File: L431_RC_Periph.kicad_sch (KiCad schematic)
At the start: 22 parts, among them J1 CAN1, J3 RC, T1 Tab, T2 Tab, T3 Tab, T4 Tab, U1 PCB

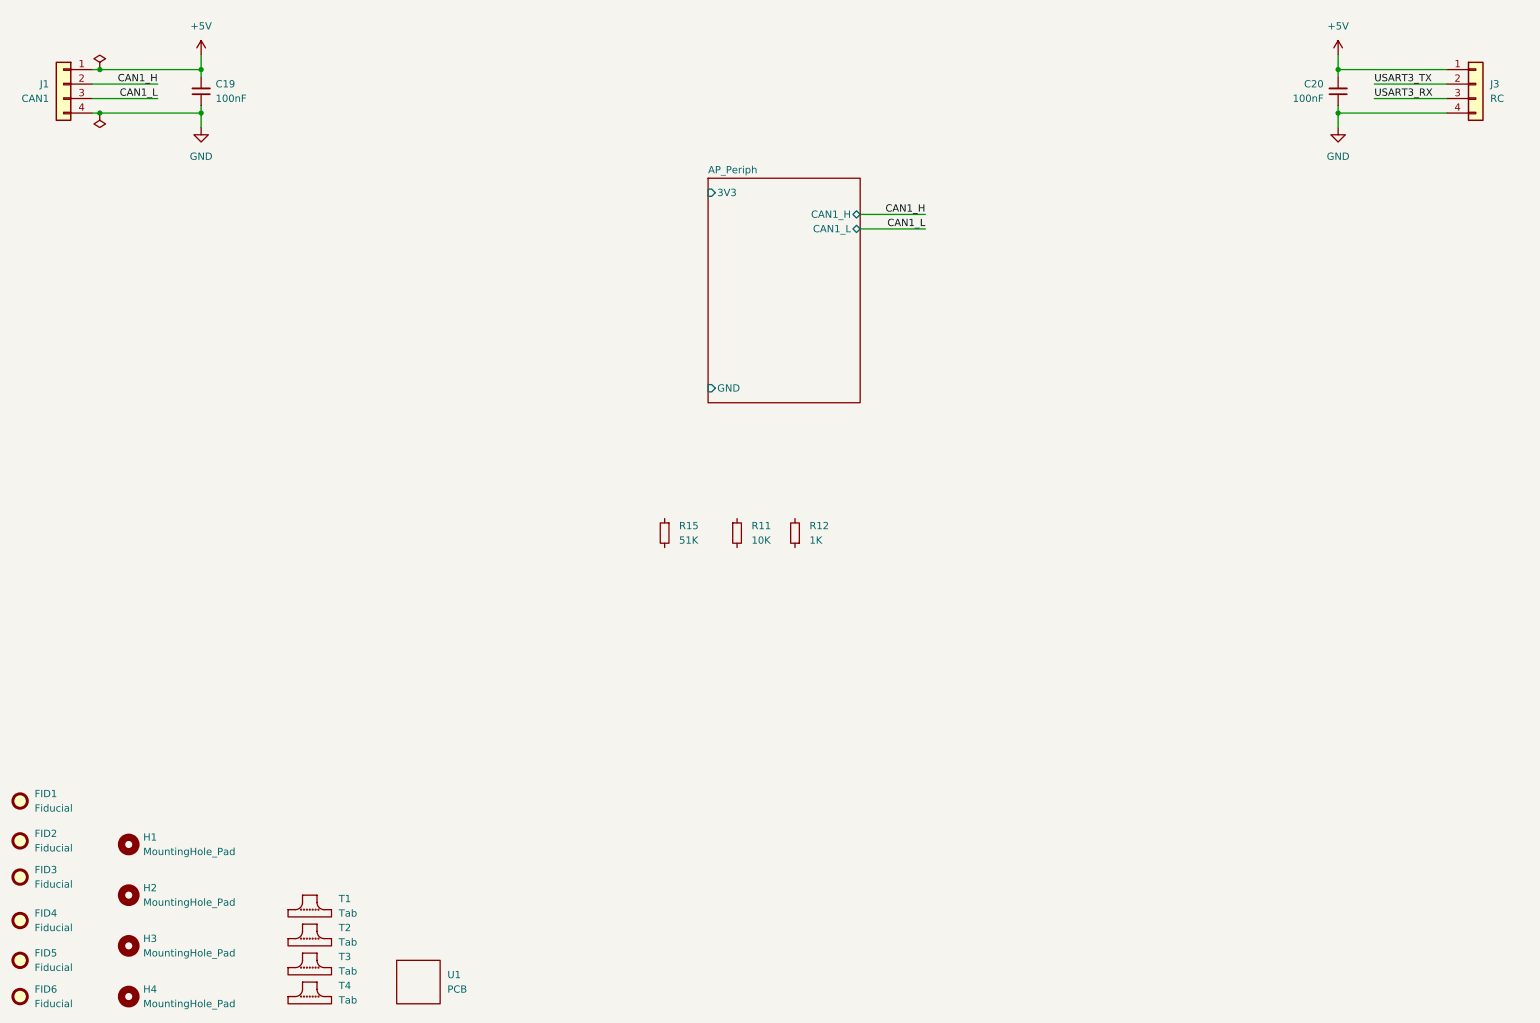
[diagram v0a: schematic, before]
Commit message: Finish routing and add option for using batt mon pads as I2C lines for added GPS
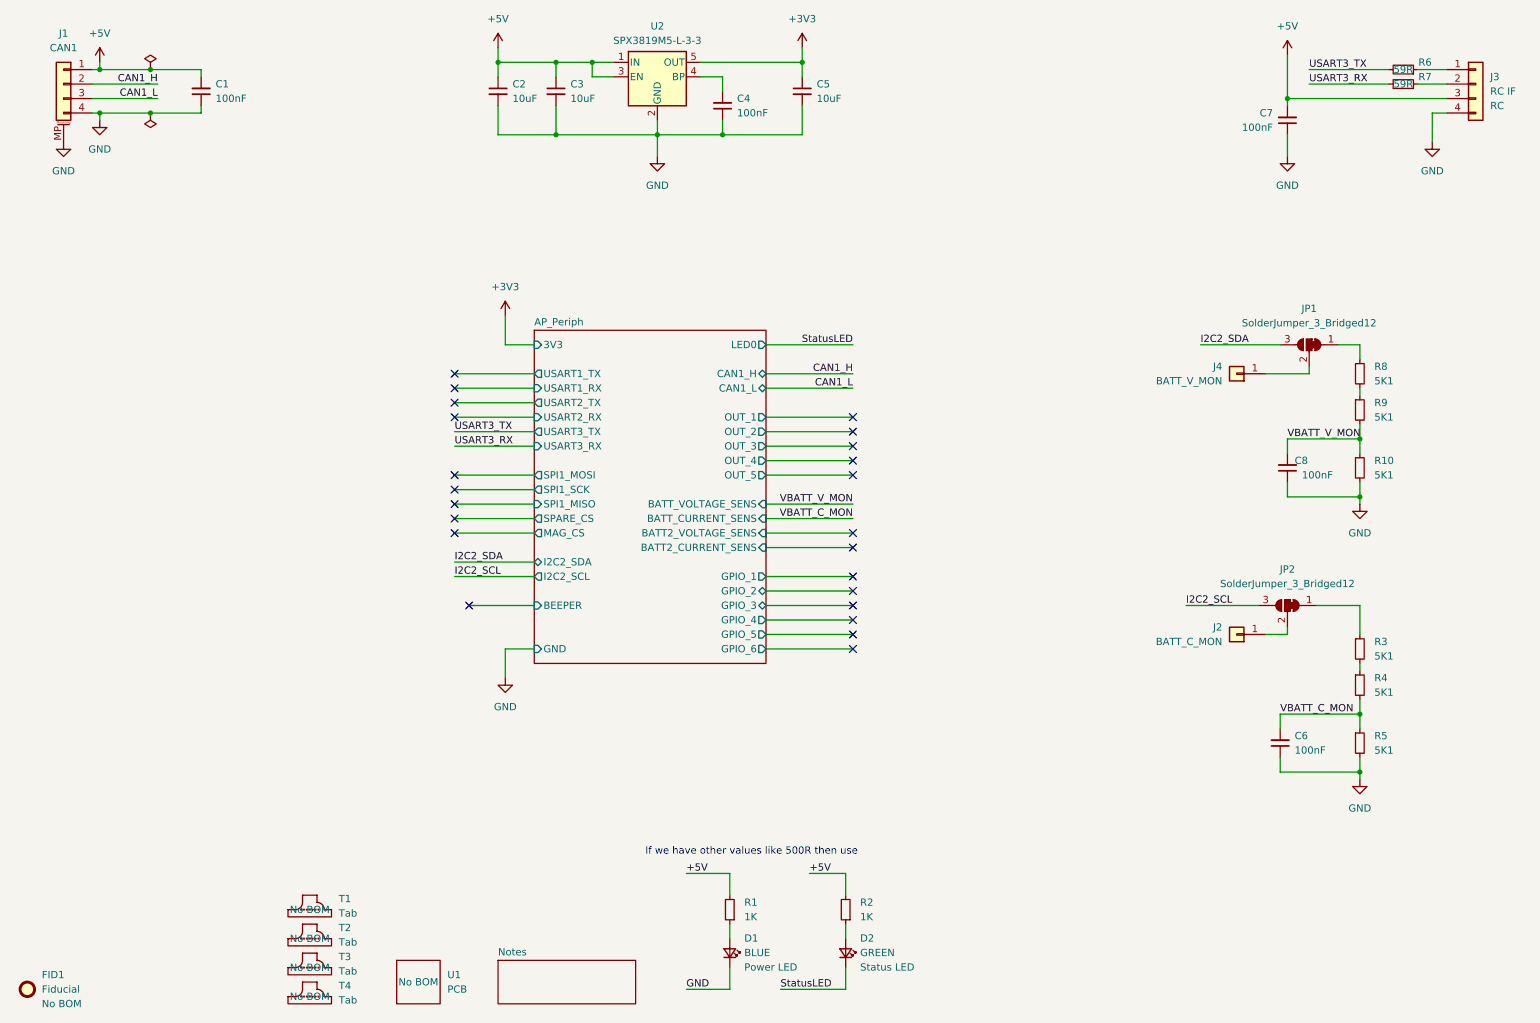
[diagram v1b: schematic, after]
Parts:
- removed FID1, FID2, FID4, FID5, FID6: Fiducial, Fiducial:Fiducial_1mm_Mask2mm, symbol Mechanical:Fiducial
- removed H1, H2, H3, H4: MountingHole_Pad, MountingHole:MountingHole_2.2mm_M2_DIN965, symbol Mechanical:MountingHole
- removed R11: 10K, Resistor_SMD:R_0402_1005Metric, symbol Device:R_Small
- removed R12: 1K, Resistor_SMD:R_0402_1005Metric, symbol Device:R_Small
- removed R15: 51K, Resistor_SMD:R_0402_1005Metric, symbol Device:R_Small
- added C2, C3, C5: 10uF, Capacitor_SMD:C_0805_2012Metric, symbol Device:C_Small
- added C4, C6, C8: 100nF, Capacitor_SMD:C_0402_1005Metric, symbol Device:C_Small
- added D1: BLUE, LED_SMD:LED_0603_1608Metric, symbol Device:LED_Small
- added D2: GREEN, LED_SMD:LED_0603_1608Metric, symbol Device:LED_Small
- added J2: BATT_C_MON, TestPoint:TestPoint_Pad_2.0x2.0mm, symbol Connector_Generic:Conn_01x01
- added J4: BATT_V_MON, TestPoint:TestPoint_Pad_2.0x2.0mm, symbol Connector_Generic:Conn_01x01
- added JP1, JP2: SolderJumper_3_Bridged12, Jumper:SolderJumper-3_P1.3mm_Bridged12_RoundedPad1.0x1.5mm, symbol Jumper:SolderJumper_3_Bridged12
- added R1, R2: 1K, Resistor_SMD:R_0402_1005Metric, symbol Device:R_Small
- added R10, R3, R4, R5, R8, R9: 5K1, Resistor_SMD:R_0402_1005Metric, symbol Device:R_Small
- added R6, R7: 59R, Resistor_SMD:R_0402_1005Metric, symbol Device:R_Small
- added U2: SPX3819M5-L-3-3, Package_TO_SOT_SMD:SOT-23-5, symbol Regulator_Linear:SPX3819M5-L-3-3
- FID1: renamed from FID3; Notes (none) -> No BOM
- J1: footprint (none) -> Connector_JST:JST_GH_SM04B-GHS-TB_1x04-1MP_P1.25mm_Horizontal; symbol Connector_Generic:Conn_01x04 -> Connector_Generic_MountingPin:Conn_01x04_MountingPin; LCSC (none) -> C189895; MPN (none) -> SM04B-GHS-TB; Price (none) -> $0.38; Supplier (none) -> Digikey; Supplier PN (none) -> 455-1566-1-ND
- J3: value RC -> RC IF; footprint (none) -> Connector_PinHeader_2.54mm:PinHeader_1x04_P2.54mm_Vertical; Interface (none) -> RC; Notes (none) -> No BOM
- T1, T2, T3, T4: Notes (none) -> No BOM
- U1: footprint Mad_Footprints:BOM -> mad_footprints:BOM; Notes (none) -> No BOM
- renumbered C19 to C1, C20 to C7
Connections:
- net +5V: now also J3.3 (Pin_3), C2.1, C3.1, R1.2, R2.2, U2.1 (IN), U2.3 (EN); no longer J3.1 (Pin_1)
- net GND: now also J1.MP (MountPin), C2.2, C3.2, C4.1, C5.2, C6.1, C8.1, D1.1 (K), R10.2, R5.2, U2.2 (GND)
- net USART3_RX: now also R7.2; no longer J3.3 (Pin_3)
- net USART3_TX: now also R6.2; no longer J3.2 (Pin_2)
- new net: J4.1 (Pin_1), JP1.2 (C)
- new net: JP2.1 (A), R3.1
- new net: R3.2, R4.1
- new net: D2.2 (A), R2.1
- new net: D1.2 (A), R1.1
- new net: JP1.1 (A), R8.1
- new net: C4.2, U2.4 (BP)
- new net: J3.1 (Pin_1), R6.1
- new net: R8.2, R9.1
- new net: J3.2 (Pin_2), R7.1
- new net: J2.1 (Pin_1), JP2.2 (C)
- new net +3V3: C5.1, U2.5 (OUT)
- new net I2C2_SCL: JP2.3 (B)
- new net I2C2_SDA: JP1.3 (B)
- new net StatusLED: D2.1 (K)
- new net VBATT_C_MON: C6.2, R4.2, R5.1
- new net VBATT_V_MON: C8.2, R10.1, R9.2
- no-connect marks 0 -> 23
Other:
- added sheet Notes (notes.kicad_sch)
- sheet AP_Periph ports: added BATT2_CURRENT_SENS, BATT2_VOLTAGE_SENS, BATT_CURRENT_SENS, BATT_VOLTAGE_SENS, BEEPER, GPIO_1, GPIO_2, GPIO_3, GPIO_4, GPIO_5, GPIO_6, I2C2_SCL, I2C2_SDA, LED0, MAG_CS, OUT_1, OUT_2, OUT_3, OUT_4, OUT_5, SPARE_CS, SPI1_MISO, SPI1_MOSI, SPI1_SCK, USART1_RX, USART1_TX, USART2_RX, USART2_TX, USART3_RX, USART3_TX; removed none
- note added: "If we have other values like 500R then use"
- moved on the sheet: C7, FID1

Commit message: Update to 6 pin headers and remove the two solder pads
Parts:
- removed FID1: Fiducial, Fiducial:Fiducial_1mm_Mask2mm, symbol Mechanical:Fiducial
- removed J2: BATT_C_MON, TestPoint:TestPoint_Pad_2.0x2.0mm, symbol Connector_Generic:Conn_01x01
- removed J4: BATT_V_MON, TestPoint:TestPoint_Pad_2.0x2.0mm, symbol Connector_Generic:Conn_01x01
- J3: footprint Connector_PinHeader_2.54mm:PinHeader_1x04_P2.54mm_Vertical -> Connector_PinHeader_2.54mm:PinHeader_1x06_P2.54mm_Vertical; symbol Connector_Generic:Conn_01x04 -> Connector_Generic:Conn_01x06
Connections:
- net Out1: now reaches JP1.2 (C)
- net Out1: now also J3.5 (Pin_5)
- net Out2: now reaches JP2.2 (C)
- net Out2: now also J3.6 (Pin_6)
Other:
- note added: "Rename to better names for Out1/Out2"
- note removed: "If we have other values like 500R then use"
